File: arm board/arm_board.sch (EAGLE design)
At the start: 96 parts, among them J1 APPPP45_PCB_HORIZ_RIGHT, J14 APPPP45_PCB_HORIZ_RIGHT, J15 APPPP45_PCB_HORIZ_RIGHT, J16 APPPP45_PCB_HORIZ_RIGHT, J17 APPPP45_PCB_HORIZ_RIGHT, J18 APPPP45_PCB_HORIZ_RIGHT, J19 ENCODER, J2 APPPP45_PCB_HORIZ_RIGHT, J20 ENCODER, J21 ENCODER, J22 ENCODER, J24 ENCODER, J3 APPPP45_PCB_HORIZ_RIGHT, Q1 Q_IRF7437SMD, U1 TIVA-1294, U3 MAX3232D

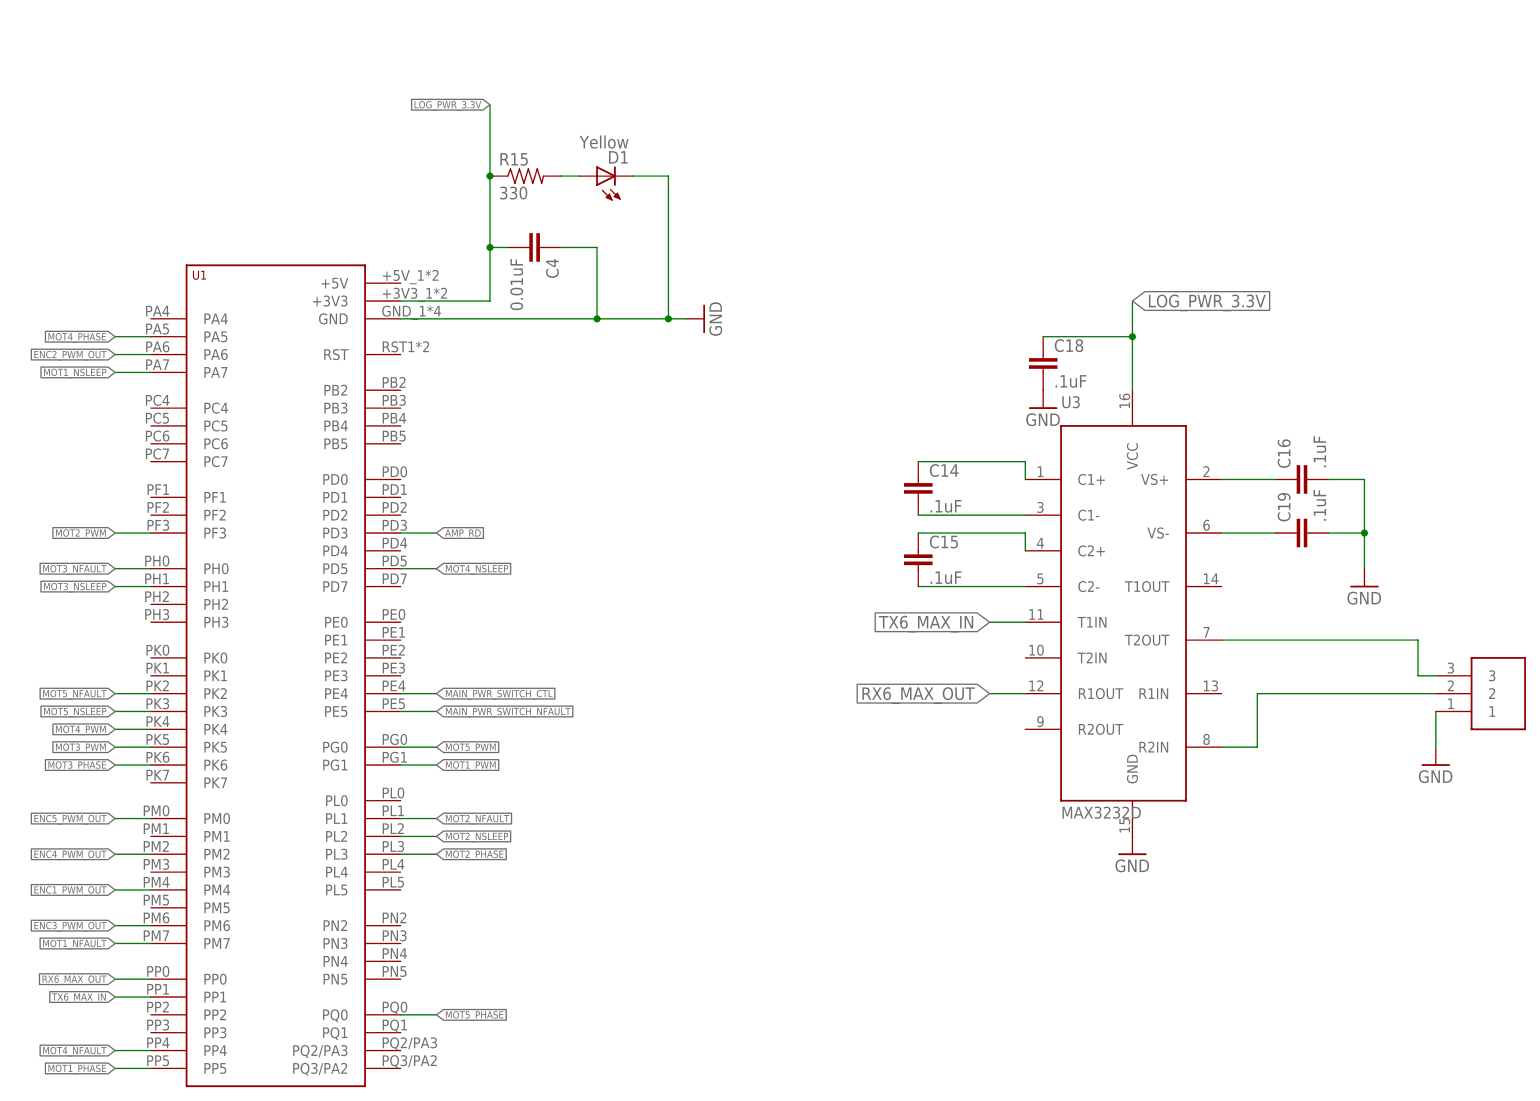
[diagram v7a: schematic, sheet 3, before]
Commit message: removed useless serial, added power header
We can use the header to disable power going to the tiva if we want to
run it off of usb while running the board
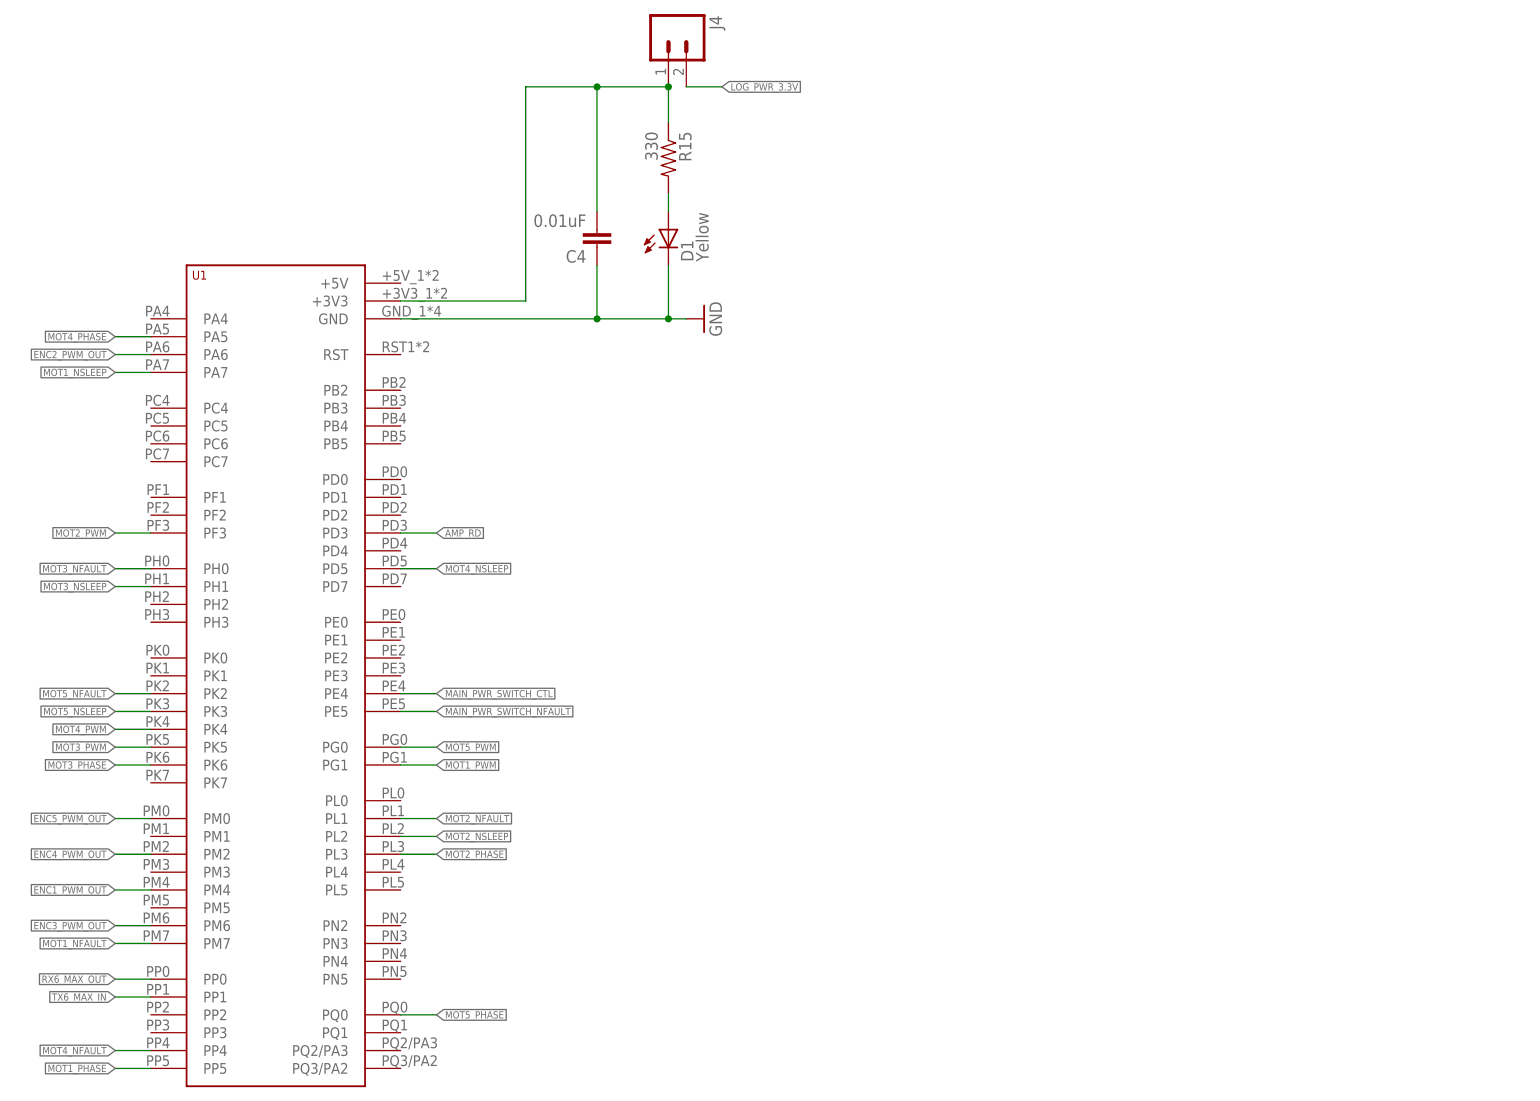
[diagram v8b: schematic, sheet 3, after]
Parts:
- removed C14, C15, C16, C18, C19: .1uF, SparkFun-Capacitors:2.2UF-25V-+80/-20(0805)
- removed RS232_IO: SL03, MRDT-Connectors:SL03
- removed U3: MAX3232D, MRDT-ICs:MAX3232D
- added J4: (no value), SparkFun-Connectors:M02PTH
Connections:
- removed net N$10: C15.2, U3.C2-
- removed net N$12: C16.1, U3.VS+
- removed net N$13: C19.1, U3.VS-
- removed net N$14: RS232_IO.3, U3.T2OUT
- removed net N$15: RS232_IO.2, U3.R2IN
- removed net N$5: C14.1, U3.C1+
- removed net N$6: C14.2, U3.C1-
- removed net N$9: C15.1, U3.C2+
- new net N$32: C4.2, J4.1, R15.1, U1.+3V3
- net GND: no longer C16.2, C18.2, C19.2, RS232_IO.1, U3.GND
- net LOG_PWR_3.3V: now also J4.2; no longer C18.1, C4.2, R15.1, U1.+3V3, U3.VCC
- net RX6_MAX_OUT: no longer U3.R1OUT
- net TX6_MAX_IN: no longer U3.T1IN
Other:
- moved on the sheet: C4, D1, R15
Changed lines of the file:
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@@
 <part name="U$11" library="mine" deviceset="APP45_HORIZ" device=""/>
 <part name="H4" library="MRDT-Hardware" deviceset="MOUNTING_HOLE" device="#4"/>
-<part name="U3" library="MRDT-ICs" deviceset="MAX*232" device="D" technology="3"/>
-<part name="C14" library="SparkFun-Capacitors" deviceset="2.2UF-25V-+80/-20(0805)" device="" value=".1uF"/>
-<part name="C15" library="SparkFun-Capacitors" deviceset="2.2UF-25V-+80/-20(0805)" device="" value=".1uF"/>
-<part name="C16" library="SparkFun-Capacitors" deviceset="2.2UF-25V-+80/-20(0805)" device="" value=".1uF"/>
-<part name="C18" library="SparkFun-Capacitors" deviceset="2.2UF-25V-+80/-20(0805)" device="" value=".1uF"/>
-<part name="GND37" library="SparkFun-Aesthetics" deviceset="GND" device=""/>
-<part name="C19" library="SparkFun-Capacitors" deviceset="2.2UF-25V-+80/-20(0805)" device="" value=".1uF"/>
-<part name="GND38" library="SparkFun-Aesthetics" deviceset="GND" device=""/>
-<part name="GND13" library="SparkFun-Aesthetics" deviceset="GND" device=""/>
-<part name="RS232_IO" library="MRDT-Connectors" deviceset="SL03" device=""/>
-<part name="GND15" library="SparkFun-Aesthetics" deviceset="GND" device=""/>
 <part name="FRAME1" library="frames" deviceset="A3L-LOC" device=""/>
 <part name="FRAME2" library="frames" deviceset="A3P-LOC" device=""/>
@@
 <part name="C12" library="SparkFun-Capacitors" deviceset="CAP_POL" device="E" value="330uF"/>
 <part name="U$13" library="MRDT-ICs" deviceset="AZ1117E" device="AZ1117EH-3.3"/>
+<part name="J4" library="SparkFun-Connectors" deviceset="M02" device="PTH"/>
 </parts>
 <sheets>
@@
 <instance part="U1" gate="G$1" x="-7.62" y="7.62"/>
 <instance part="GND12" gate="1" x="66.04" y="116.84" rot="R90"/>
-<instance part="C4" gate="G$1" x="40.64" y="127" rot="R270"/>
-<instance part="U3" gate="G$1" x="127" y="76.2"/>
-<instance part="C14" gate="G$1" x="96.52" y="91.44"/>
-<instance part="C15" gate="G$1" x="96.52" y="81.28"/>
-<instance part="C16" gate="G$1" x="152.4" y="93.98" rot="R90"/>
-<instance part="C18" gate="G$1" x="114.3" y="109.22"/>
-<instance part="GND37" gate="1" x="114.3" y="104.14"/>
-<instance part="C19" gate="G$1" x="152.4" y="86.36" rot="R90"/>
-<instance part="GND38" gate="1" x="160.02" y="78.74"/>
-<instance part="GND13" gate="1" x="127" y="40.64"/>
-<instance part="RS232_IO" gate="G$1" x="177.8" y="63.5"/>
-<instance part="GND15" gate="1" x="170.18" y="53.34"/>
+<instance part="C4" gate="G$1" x="50.8" y="129.54" rot="R180"/>
 <instance part="FRAME3" gate="G$1" x="-99.06" y="-20.32"/>
-<instance part="D1" gate="G$1" x="50.8" y="137.16" rot="R90"/>
-<instance part="R15" gate="G$1" x="40.64" y="137.16"/>
+<instance part="D1" gate="G$1" x="60.96" y="129.54"/>
+<instance part="R15" gate="G$1" x="60.96" y="139.7" rot="R270"/>
+<instance part="J4" gate="G$1" x="60.96" y="157.48" rot="R270"/>
 </instances>
 <busses>
@@
 <wire x1="50.8" y1="116.84" x2="60.96" y2="116.84" width="0.1524" layer="91"/>
 <wire x1="60.96" y1="116.84" x2="63.5" y2="116.84" width="0.1524" layer="91"/>
-<wire x1="45.72" y1="127" x2="50.8" y2="127" width="0.1524" layer="91"/>
-<wire x1="50.8" y1="127" x2="50.8" y2="116.84" width="0.1524" layer="91"/>
+<wire x1="50.8" y1="124.46" x2="50.8" y2="116.84" width="0.1524" layer="91"/>
 <junction x="50.8" y="116.84"/>
-<wire x1="60.96" y1="137.16" x2="60.96" y2="116.84" width="0.1524" layer="91"/>
+<wire x1="60.96" y1="124.46" x2="60.96" y2="116.84" width="0.1524" layer="91"/>
 <junction x="60.96" y="116.84"/>
 <pinref part="D1" gate="G$1" pin="C"/>
-<wire x1="55.88" y1="137.16" x2="60.96" y2="137.16" width="0.1524" layer="91"/>
-</segment>
-<segment>
-<pinref part="C18" gate="G$1" pin="2"/>
-<pinref part="GND37" gate="1" pin="GND"/>
-</segment>
-<segment>
-<pinref part="C16" gate="G$1" pin="2"/>
-<pinref part="GND38" gate="1" pin="GND"/>
-<wire x1="154.94" y1="93.98" x2="160.02" y2="93.98" width="0.1524" layer="91"/>
-<wire x1="160.02" y1="93.98" x2="160.02" y2="86.36" width="0.1524" layer="91"/>
-<pinref part="C19" gate="G$1" pin="2"/>
-<wire x1="160.02" y1="86.36" x2="160.02" y2="81.28" width="0.1524" layer="91"/>
-<wire x1="154.94" y1="86.36" x2="160.02" y2="86.36" width="0.1524" layer="91"/>
-<junction x="160.02" y="86.36"/>
-</segment>
-<segment>
-<pinref part="U3" gate="G$1" pin="GND"/>
-<pinref part="GND13" gate="1" pin="GND"/>
-</segment>
-<segment>
-<pinref part="RS232_IO" gate="G$1" pin="1"/>
-<pinref part="GND15" gate="1" pin="GND"/>
-<wire x1="170.18" y1="60.96" x2="170.18" y2="55.88" width="0.1524" layer="91"/>
 </segment>
 </net>
 <net name="LOG_PWR_3.3V" class="0">
 <segment>
-<label x="35.56" y="147.32" size="1.016" layer="95" rot="R180" xref="yes"/>
-<pinref part="U1" gate="G$1" pin="+3V3"/>
-<wire x1="22.86" y1="119.38" x2="35.56" y2="119.38" width="0.1524" layer="91"/>
-<wire x1="35.56" y1="147.32" x2="35.56" y2="137.16" width="0.1524" layer="91"/>
-<pinref part="C4" gate="G$1" pin="2"/>
-<wire x1="35.56" y1="137.16" x2="35.56" y2="127" width="0.1524" layer="91"/>
-<wire x1="35.56" y1="127" x2="35.56" y2="119.38" width="0.1524" layer="91"/>
-<wire x1="38.1" y1="127" x2="35.56" y2="127" width="0.1524" layer="91"/>
-<junction x="35.56" y="127"/>
-<pinref part="R15" gate="G$1" pin="1"/>
-<junction x="35.56" y="137.16"/>
-</segment>
-<segment>
-<pinref part="U3" gate="G$1" pin="VCC"/>
-<wire x1="127" y1="106.68" x2="127" y2="114.3" width="0.1524" layer="91"/>
-<label x="127" y="119.38" size="1.778" layer="95" xref="yes"/>
-<pinref part="C18" gate="G$1" pin="1"/>
-<wire x1="127" y1="114.3" x2="127" y2="119.38" width="0.1524" layer="91"/>
-<wire x1="114.3" y1="114.3" x2="127" y2="114.3" width="0.1524" layer="91"/>
-<junction x="127" y="114.3"/>
+<label x="68.58" y="149.86" size="1.016" layer="95" xref="yes"/>
+<wire x1="63.5" y1="149.86" x2="68.58" y2="149.86" width="0.1524" layer="91"/>
+<pinref part="J4" gate="G$1" pin="2"/>
 </segment>
 </net>
@@
 <label x="-17.78" y="22.86" size="1.016" layer="95" rot="R180" xref="yes"/>
 </segment>
-<segment>
-<pinref part="U3" gate="G$1" pin="R1OUT"/>
-<wire x1="111.76" y1="63.5" x2="106.68" y2="63.5" width="0.1524" layer="91"/>
-<label x="106.68" y="63.5" size="1.778" layer="95" rot="R180" xref="yes"/>
-</segment>
 </net>
 <net name="TX6_MAX_IN" class="0">
@@
 <label x="-17.78" y="20.32" size="1.016" layer="95" rot="R180" xref="yes"/>
 </segment>
-<segment>
-<pinref part="U3" gate="G$1" pin="T1IN"/>
-<wire x1="111.76" y1="73.66" x2="106.68" y2="73.66" width="0.1524" layer="91"/>
-<label x="106.68" y="73.66" size="1.778" layer="95" rot="R180" xref="yes"/>
-</segment>
 </net>
 <net name="ENC1_PWM_OUT" class="0">
@@
 </segment>
 </net>
-<net name="N$5" class="0">
-<segment>
-<pinref part="C14" gate="G$1" pin="1"/>
-<pinref part="U3" gate="G$1" pin="C1+"/>
-<wire x1="96.52" y1="96.52" x2="111.76" y2="96.52" width="0.1524" layer="91"/>
-<wire x1="111.76" y1="96.52" x2="111.76" y2="93.98" width="0.1524" layer="91"/>
-</segment>
-</net>
-<net name="N$6" class="0">
-<segment>
-<pinref part="U3" gate="G$1" pin="C1-"/>
-<pinref part="C14" gate="G$1" pin="2"/>
-<wire x1="111.76" y1="88.9" x2="96.52" y2="88.9" width="0.1524" layer="91"/>
-</segment>
-</net>
-<net name="N$9" class="0">
-<segment>
-<pinref part="C15" gate="G$1" pin="1"/>
-<pinref part="U3" gate="G$1" pin="C2+"/>
-<wire x1="96.52" y1="86.36" x2="111.76" y2="86.36" width="0.1524" layer="91"/>
-<wire x1="111.76" y1="86.36" x2="111.76" y2="83.82" width="0.1524" layer="91"/>
-</segment>
-</net>
-<net name="N$10" class="0">
-<segment>
-<pinref part="C15" gate="G$1" pin="2"/>
-<pinref part="U3" gate="G$1" pin="C2-"/>
-<wire x1="96.52" y1="78.74" x2="111.76" y2="78.74" width="0.1524" layer="91"/>
-</segment>
-</net>
-<net name="N$12" class="0">
-<segment>
-<pinref part="U3" gate="G$1" pin="VS+"/>
-<pinref part="C16" gate="G$1" pin="1"/>
-<wire x1="139.7" y1="93.98" x2="147.32" y2="93.98" width="0.1524" layer="91"/>
-</segment>
-</net>
-<net name="N$13" class="0">
-<segment>
-<pinref part="U3" gate="G$1" pin="VS-"/>
-<pinref part="C19" gate="G$1" pin="1"/>
-<wire x1="139.7" y1="86.36" x2="147.32" y2="86.36" width="0.1524" layer="91"/>
-</segment>
-</net>
-<net name="N$14" class="0">
-<segment>
-<pinref part="U3" gate="G$1" pin="T2OUT"/>
-<wire x1="139.7" y1="71.12" x2="167.64" y2="71.12" width="0.1524" layer="91"/>
-<wire x1="167.64" y1="71.12" x2="167.64" y2="66.04" width="0.1524" layer="91"/>
-<pinref part="RS232_IO" gate="G$1" pin="3"/>
-<wire x1="167.64" y1="66.04" x2="170.18" y2="66.04" width="0.1524" layer="91"/>
-</segment>
-</net>
-<net name="N$15" class="0">
-<segment>
-<pinref part="RS232_IO" gate="G$1" pin="2"/>
-<wire x1="170.18" y1="63.5" x2="144.78" y2="63.5" width="0.1524" layer="91"/>
-<wire x1="144.78" y1="63.5" x2="144.78" y2="55.88" width="0.1524" layer="91"/>
-<pinref part="U3" gate="G$1" pin="R2IN"/>
-<wire x1="144.78" y1="55.88" x2="139.7" y2="55.88" width="0.1524" layer="91"/>
-</segment>
-</net>
 <net name="ENC5_PWM_OUT" class="0">
 <segment>
@@
 <pinref part="R15" gate="G$1" pin="2"/>
 <pinref part="D1" gate="G$1" pin="A"/>
-<wire x1="45.72" y1="137.16" x2="48.26" y2="137.16" width="0.1524" layer="91"/>
-</segment>
-</net>
+<wire x1="60.96" y1="134.62" x2="60.96" y2="132.08" width="0.1524" layer="91"/>
+</segment>
+</net>
+<net name="N$32" class="0">
+<segment>
+<pinref part="U1" gate="G$1" pin="+3V3"/>
+<wire x1="40.64" y1="119.38" x2="22.86" y2="119.38" width="0.1524" layer="91"/>
+<pinref part="J4" gate="G$1" pin="1"/>
+<wire x1="60.96" y1="149.86" x2="50.8" y2="149.86" width="0.1524" layer="91"/>
+<wire x1="50.8" y1="149.86" x2="40.64" y2="149.86" width="0.1524" layer="91"/>
+<wire x1="40.64" y1="149.86" x2="40.64" y2="119.38" width="0.1524" layer="91"/>
+<pinref part="R15" gate="G$1" pin="1"/>
+<wire x1="60.96" y1="144.78" x2="60.96" y2="149.86" width="0.1524" layer="91"/>
+<junction x="60.96" y="149.86"/>
+<pinref part="C4" gate="G$1" pin="2"/>
+<wire x1="50.8" y1="132.08" x2="50.8" y2="149.86" width="0.1524" layer="91"/>
+<junction x="50.8" y="149.86"/>
+</segment>
+</net>
